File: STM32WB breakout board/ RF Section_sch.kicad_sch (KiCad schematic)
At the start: 12 parts, among them J3 RSP-122811-02

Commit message: Temp
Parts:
- FL1: footprint DLF162500LT5028A1 -> Filter:DLF162500LT5028A1
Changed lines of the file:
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@@
       (effects (font (size 1.27 1.27)))
     )
-    (property "Footprint" "DLF162500LT5028A1" (at 144.018 125.908 0)
+    (property "Footprint" "Filter:DLF162500LT5028A1" (at 144.018 125.908 0)
       (effects (font (size 1.27 1.27)) (justify left top) hide)
     )

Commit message: PCB SMPS section inductors updated
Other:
- note added: "SMPS Section"
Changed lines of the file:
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@@
     (fill (type none))
+  )
+  (text "SMPS Section" (at 72.263 83.058 0)
+    (effects (font (size 2.54 2.54)) (justify left bottom))
   )
   (text "10 uH" (at 30.988 107.95 90)

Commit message: USB excluded
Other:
- moved on the sheet: C11, C7

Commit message: PCB button updated
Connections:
- net VFBSMPS: now also L3.2; no longer L3.1
- net VLXSMPS: now also L2.1; no longer L2.2
- new net: L2.2, L3.1
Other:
- moved on the sheet: L3
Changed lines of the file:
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@@
     (effects (font (size 2.54 2.54)) (justify left bottom))
   )
-  (text "10 uH" (at 30.988 107.95 90)
+  (text "10 uH" (at 32.004 107.95 90)
     (effects (font (size 1.27 1.27)) (justify left bottom))
   )
@@
     )
   )
-  (symbol (lib_id "LQM21FN100M70L:LQM21FN100M70L") (at 28.448 105.156 90) (unit 1)
-    (in_bom yes) (on_board yes) (dnp no)
-    (property "Reference" "L3" (at 23.368 103.886 0)
+  (symbol (lib_id "LQM21FN100M70L:LQM21FN100M70L") (at 28.448 105.156 270) (unit 1)
+    (in_bom yes) (on_board yes) (dnp no)
+    (property "Reference" "L3" (at 23.241 106.299 0)
       (effects (font (size 1.27 1.27)) (justify right))
     )
-    (property "Value" "LQM21FN100M70L" (at 25.654 96.774 0)
+    (property "Value" "LQM21FN100M70L" (at 25.908 113.792 0)
       (effects (font (size 1.27 1.27)) (justify right))
     )
@@
     )
   )
-  (symbol (lib_id "LQG15WZ10NJ02D:LQG15WZ10NJ02D") (at 44.196 93.726 0) (unit 1)
-    (in_bom yes) (on_board yes) (dnp no) (fields_autoplaced)
-    (property "Reference" "L2" (at 44.196 87.63 0)
+  (symbol (lib_id "LQG15WZ10NJ02D:LQG15WZ10NJ02D") (at 44.196 93.726 0) (mirror y) (unit 1)
+    (in_bom yes) (on_board yes) (dnp no)
+    (property "Reference" "L2" (at 44.196 88.519 0)
       (effects (font (size 1.27 1.27)))
     )
-    (property "Value" "LQG15WZ10NJ02D" (at 44.196 90.17 0)
+    (property "Value" "LQG15WZ10NJ02D" (at 44.577 90.932 0)
       (effects (font (size 1.27 1.27)))
     )

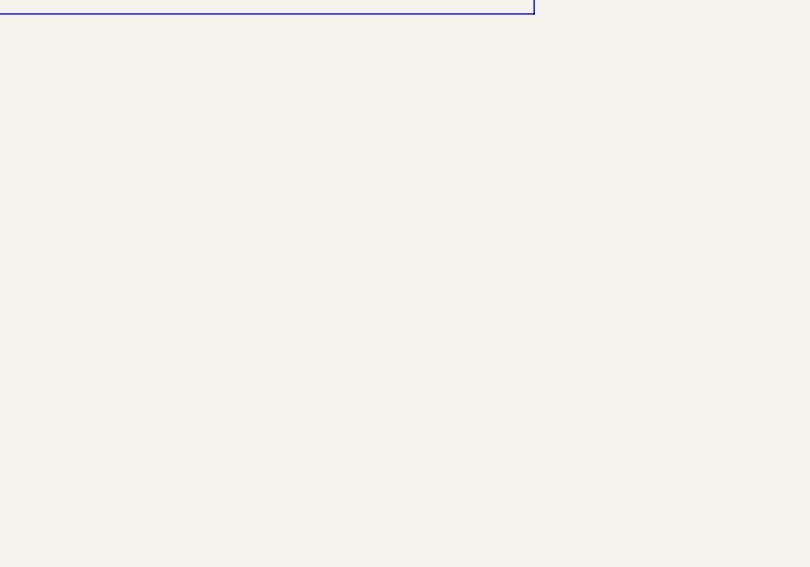
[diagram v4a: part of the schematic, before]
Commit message: Regulator section updating
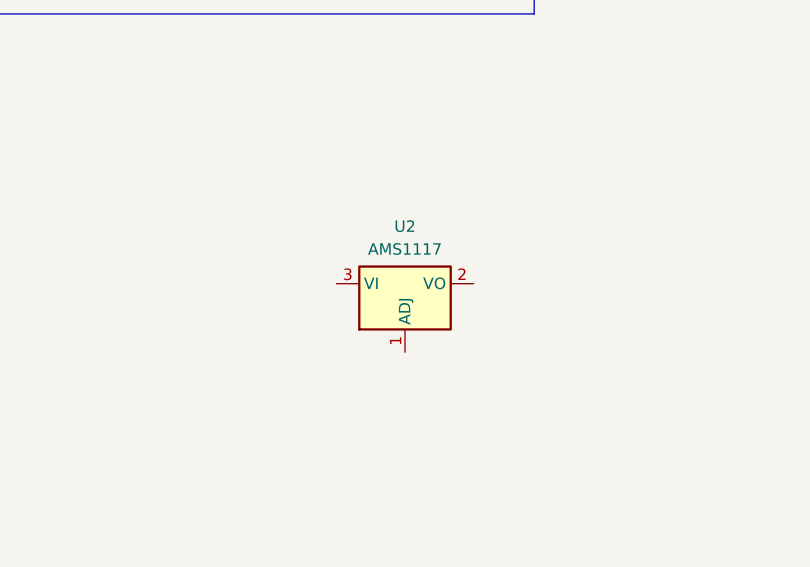
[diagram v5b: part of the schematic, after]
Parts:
- added U2: AMS1117, Package_TO_SOT_SMD:SOT-223-3_TabPin2, symbol Regulator_Linear:AMS1117
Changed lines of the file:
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@@
+    )
+  )
+  (symbol (lib_id "Regulator_Linear:AMS1117") (at 200.025 105.41 0) (unit 1)
+    (in_bom yes) (on_board yes) (dnp no) (fields_autoplaced)
+    (property "Reference" "U2" (at 200.025 99.06 0)
+      (effects (font (size 1.27 1.27)))
+    )
+    (property "Value" "AMS1117" (at 200.025 101.6 0)
+      (effects (font (size 1.27 1.27)))
+    )
+    (property "Footprint" "Package_TO_SOT_SMD:SOT-223-3_TabPin2" (at 200.025 100.33 0)
+      (effects (font (size 1.27 1.27)) hide)
+    )
+    (property "Datasheet" "http://www.advanced-monolithic.com/pdf/ds1117.pdf" (at 202.565 111.76 0)
+      (effects (font (size 1.27 1.27)) hide)
+    )
+    (pin "1")
+    (pin "2")
+    (pin "3")
+    (instances
+      (project "STM32WB breakout board"
+        (path "/29424def-bd0e-47af-8787-429d3d525da1/1e4823cc-51de-4557-be75-82cccb133913"
+          (reference "U2") (unit 1)
+        )
+      )
     )
   )
